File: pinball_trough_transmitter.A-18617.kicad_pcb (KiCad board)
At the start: 2 copper layers, 162.6 x 38.1 mm, 8 parts, among them J1 Conn_01x09_Male

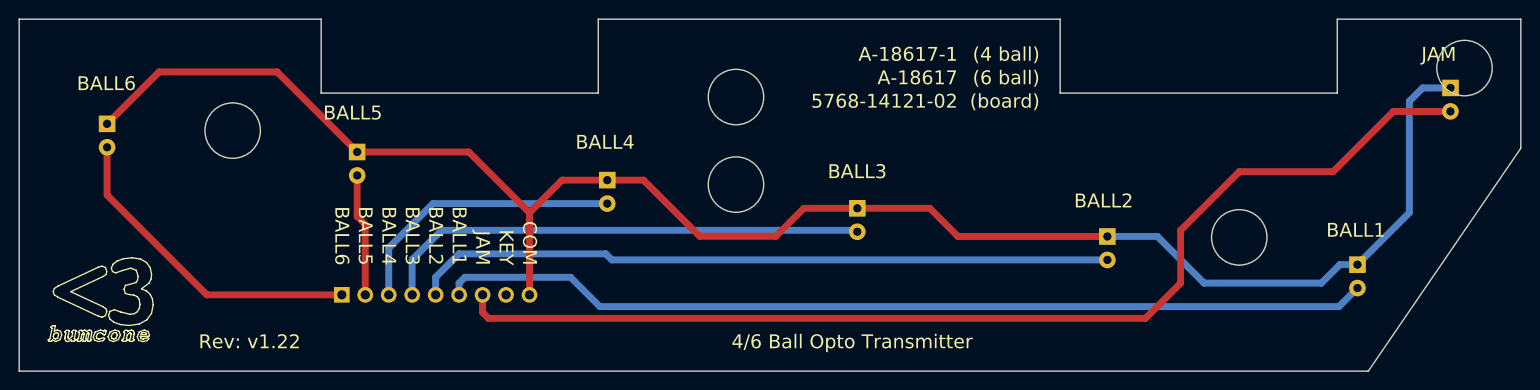
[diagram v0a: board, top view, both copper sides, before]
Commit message: Move JAM LED
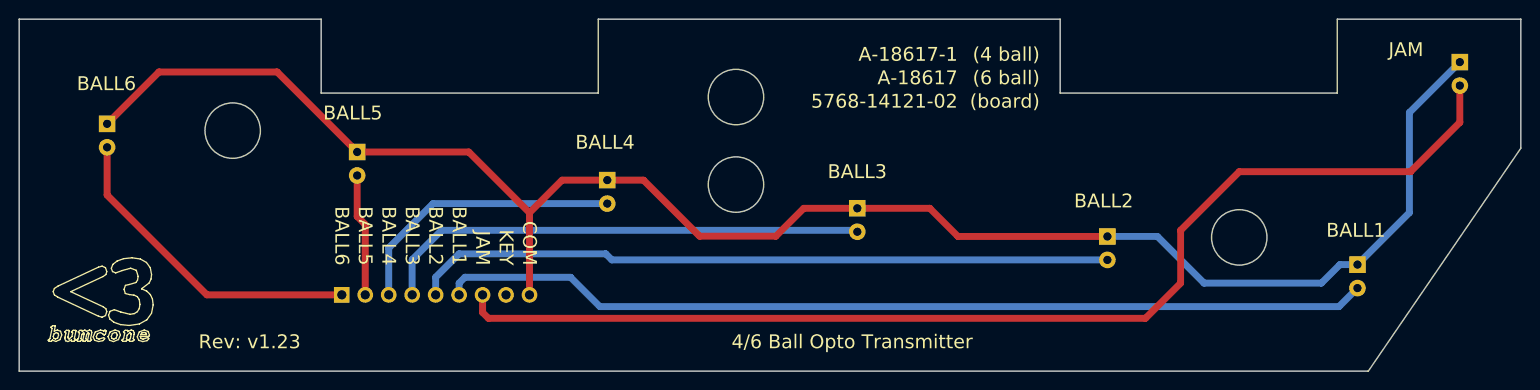
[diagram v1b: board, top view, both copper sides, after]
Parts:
- moved D1 2.97 mm to (219.5, 84.7)
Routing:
- net Net-(D1-Pad2): track 119.6 -> 124.1 mm
- net Net-(D1-Pad1): track 187.3 -> 188.8 mm
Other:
- outline, holes or cut-outs redrawn
- board text added: "Rev: v1.23"
- board text removed: "Rev: v1.22"
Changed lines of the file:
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@@
   (general
     (thickness 1.6)
-    (drawings 602)
-    (tracks 58)
+    (drawings 600)
+    (tracks 57)
     (zones 0)
     (modules 8)
@@
   (page A4)
   (title_block
-    (rev v1.22)
+    (rev v1.23)
   )
   (layers
@@
   )
   (module LED_THT:LED_D5.0mm_Clear (layer B.Cu)
-    (at 218.44 87.455 270)
+    (at 219.456 84.661 270)
     (descr "LED, diameter 5.0mm, 2 pins, http://cdn-reichelt.de/documents/datenblatt/A500/LL-504BC2E-009.pdf")
     (tags "LED diameter 5.0mm 2 pins")
@@
     )
   )
-  (gr_circle (center 219.964 85.304) (end 222.964 85.304) (layer Edge.Cuts) (width 0.15))
   (gr_text "4/6 Ball Opto Transmitter" (at 153.67 114.935) (layer F.SilkS)
     (effects (font (size 1.5 1.5) (thickness 0.3)))
@@
     (effects (font (size 1.5 1.5) (thickness 0.3)) (justify right))
   )
-  (gr_text JAM (at 219.075 83.82) (layer F.SilkS)
+  (gr_text JAM (at 215.519 83.312) (layer F.SilkS)
     (effects (font (size 1.5 1.5) (thickness 0.3)) (justify right))
   )
@@
   (gr_line (start 69.492244 107.223267) (end 68.579256 106.969267) (layer B.SilkS) (width 0.1))
   (gr_line (start 76.835 109.855) (end 76.454 110.107589) (layer B.SilkS) (width 0.1))
-  (gr_text "Rev: v1.22" (at 81.915 114.935) (layer B.SilkS)
+  (gr_text "Rev: v1.23" (at 81.915 114.935) (layer B.SilkS)
     (effects (font (size 1.5 1.5) (thickness 0.3)) (justify right mirror))
   )
@@
     (effects (font (size 1.5 1.5) (thickness 0.3)) (justify right))
   )
-  (gr_text "Rev: v1.22" (at 93.98 114.935) (layer F.SilkS)
-    (effects (font (size 1.5 1.5) (thickness 0.3)) (justify right))
-  )
-  (gr_text JAM (at 214.63 83.82) (layer B.SilkS)
+  (gr_text "Rev: v1.23" (at 93.98 114.935) (layer F.SilkS)
+    (effects (font (size 1.5 1.5) (thickness 0.3)) (justify right))
+  )
+  (gr_text JAM (at 211.074 83.312) (layer B.SilkS)
     (effects (font (size 1.5 1.5) (thickness 0.3)) (justify right mirror))
   )
@@
   (gr_line (start 95.885 107.315) (end 95.885 114.935) (layer B.SilkS) (width 0.2))
   (gr_line (start 120.015 107.315) (end 95.885 107.315) (layer B.SilkS) (width 0.2))
-  (gr_line (start 214.63 84.915) (end 214.63 92.535) (layer B.SilkS) (width 0.15))
-  (gr_line (start 222.25 84.915) (end 214.63 84.915) (layer B.SilkS) (width 0.15))
+  (gr_line (start 215.646 82.121) (end 215.646 89.741) (layer B.SilkS) (width 0.15))
+  (gr_line (start 223.266 82.121) (end 215.646 82.121) (layer B.SilkS) (width 0.15))
   (gr_line (start 204.565 104.14) (end 204.565 111.76) (layer B.SilkS) (width 0.15))
   (gr_line (start 212.185 104.14) (end 204.565 104.14) (layer B.SilkS) (width 0.15))
@@
   (segment (start 165.127 103.532) (end 181.304 103.532) (width 0.75) (layer F.Cu) (net 1))
   (segment (start 162.079 100.484) (end 165.127 103.532) (width 0.75) (layer F.Cu) (net 1))
-  (segment (start 218.44 87.455) (end 215.44 87.455) (width 0.75) (layer B.Cu) (net 1))
-  (segment (start 215.44 87.455) (end 213.995 88.9) (width 0.75) (layer B.Cu) (net 1))
   (segment (start 213.995 100.96) (end 208.375 106.58) (width 0.75) (layer B.Cu) (net 1))
-  (segment (start 213.995 88.9) (end 213.995 100.96) (width 0.75) (layer B.Cu) (net 1))
   (segment (start 206.475 106.58) (end 208.375 106.58) (width 0.75) (layer B.Cu) (net 1))
   (segment (start 204.47 108.585) (end 206.475 106.58) (width 0.75) (layer B.Cu) (net 1))
@@
   (segment (start 186.717 103.532) (end 191.77 108.585) (width 0.75) (layer B.Cu) (net 1))
   (segment (start 181.304 103.532) (end 186.717 103.532) (width 0.75) (layer B.Cu) (net 1))
-  (segment (start 218.44 89.995) (end 212.265 89.995) (width 0.75) (layer F.Cu) (net 2))
-  (segment (start 212.265 89.995) (end 205.74 96.52) (width 0.75) (layer F.Cu) (net 2))
-  (segment (start 205.74 96.52) (end 195.58 96.52) (width 0.75) (layer F.Cu) (net 2))
+  (segment (start 213.995 90.122) (end 219.456 84.661) (width 0.75) (layer B.Cu) (net 1))
+  (segment (start 213.995 100.96) (end 213.995 90.122) (width 0.75) (layer B.Cu) (net 1))
   (segment (start 195.58 96.52) (end 189.23 102.87) (width 0.75) (layer F.Cu) (net 2))
   (segment (start 189.23 102.87) (end 189.23 108.585) (width 0.75) (layer F.Cu) (net 2))
@@
   (segment (start 113.665 111.76) (end 113.665 109.855) (width 0.75) (layer F.Cu) (net 2))
   (segment (start 114.3 112.395) (end 113.665 111.76) (width 0.75) (layer F.Cu) (net 2))
+  (segment (start 195.58 96.52) (end 214.122 96.52) (width 0.75) (layer F.Cu) (net 2))
+  (segment (start 219.456 91.186) (end 219.456 87.201) (width 0.75) (layer F.Cu) (net 2))
+  (segment (start 214.122 96.52) (end 219.456 91.186) (width 0.75) (layer F.Cu) (net 2))
   (segment (start 206.37 111.125) (end 208.375 109.12) (width 0.75) (layer B.Cu) (net 3))
   (segment (start 126.365 111.125) (end 123.19 107.95) (width 0.75) (layer B.Cu) (net 3))

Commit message: Move J1 header back a little
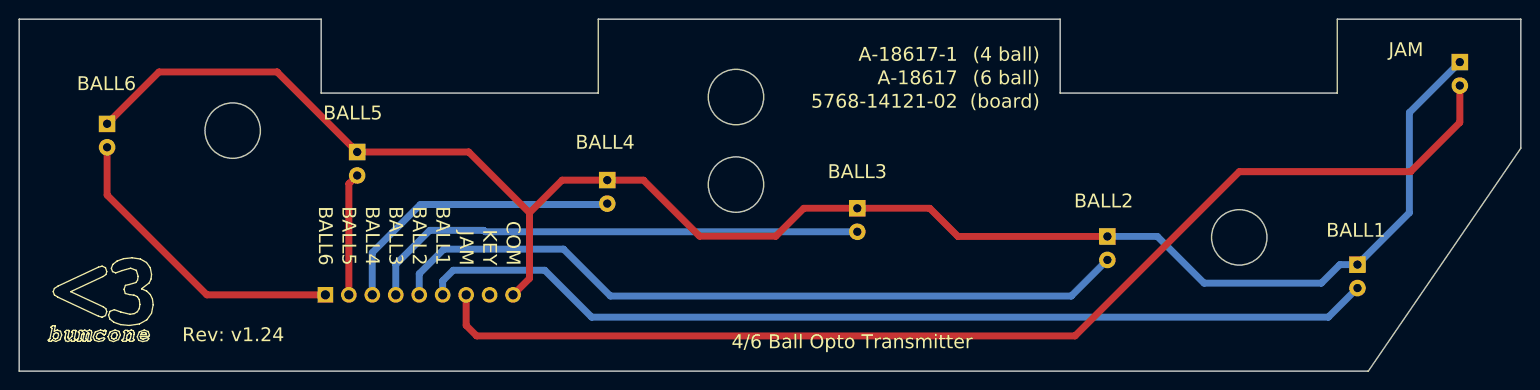
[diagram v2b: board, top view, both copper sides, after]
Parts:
- moved J1 1.78 mm to (96.6, 109.9)
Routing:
- net Net-(D3-Pad2): track 76.0 -> 81.6 mm
- net Net-(D2-Pad2): track 100.9 -> 104.4 mm
- net Net-(D7-Pad2): track 35.1 -> 33.3 mm
- net Net-(D4-Pad2): track 53.4 -> 55.1 mm
- net Net-(D5-Pad2): track 30.7 -> 32.2 mm
- net Net-(D1-Pad2): track 124.1 -> 124.9 mm
- net Net-(D1-Pad1): track 188.8 -> 189.5 mm
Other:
- board text added: "Rev: v1.24"
- board text removed: "Rev: v1.23"

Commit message: Use Molex connector
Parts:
- J1: value Conn_01x09_Male -> Molex 22-05-3091
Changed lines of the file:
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@@
       (effects (font (size 1 1) (thickness 0.15)) (justify mirror))
     )
-    (fp_text value Conn_01x09_Male (at -3.175 -9.525) (layer B.Fab)
+    (fp_text value "Molex 22-05-3091" (at -3.175 -9.525) (layer B.Fab)
       (effects (font (size 1 1) (thickness 0.15)) (justify mirror))
     )
@@
     (pad 1 thru_hole rect (at 0 0 270) (size 1.7 1.7) (drill 1) (layers *.Cu *.Mask)
       (net 8 "Net-(D7-Pad2)"))
-    (model ${KISYS3DMOD}/Connector_PinHeader_2.54mm.3dshapes/PinHeader_1x09_P2.54mm_Horizontal.wrl
+    (model ${KIPRJMOD}/kicad/libs/packages3d/Molex/22-05-3091.step
       (at (xyz 0 0 0))
       (scale (xyz 1 1 1))

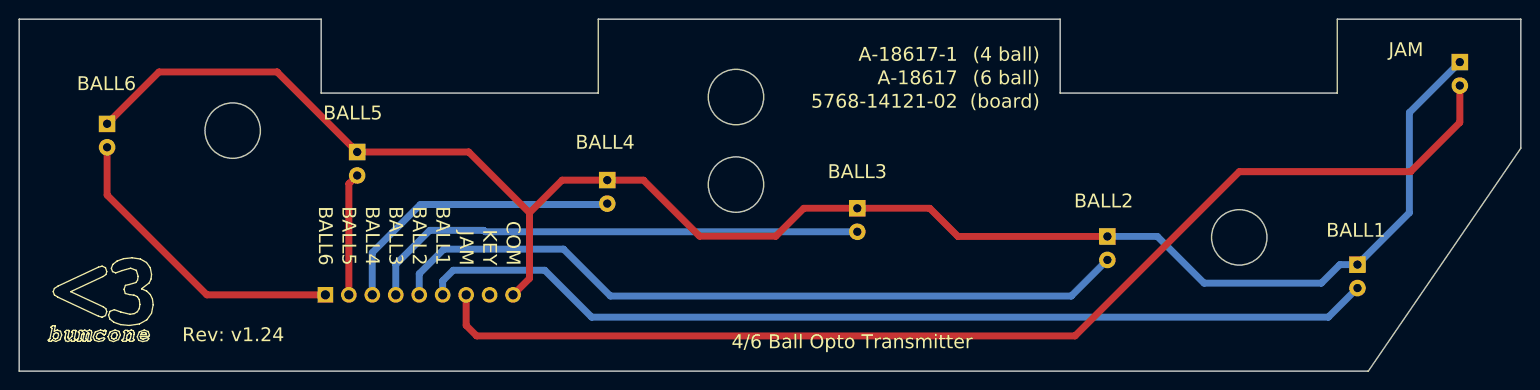
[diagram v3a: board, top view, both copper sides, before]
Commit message: Align LEDs with the center of the trough holes
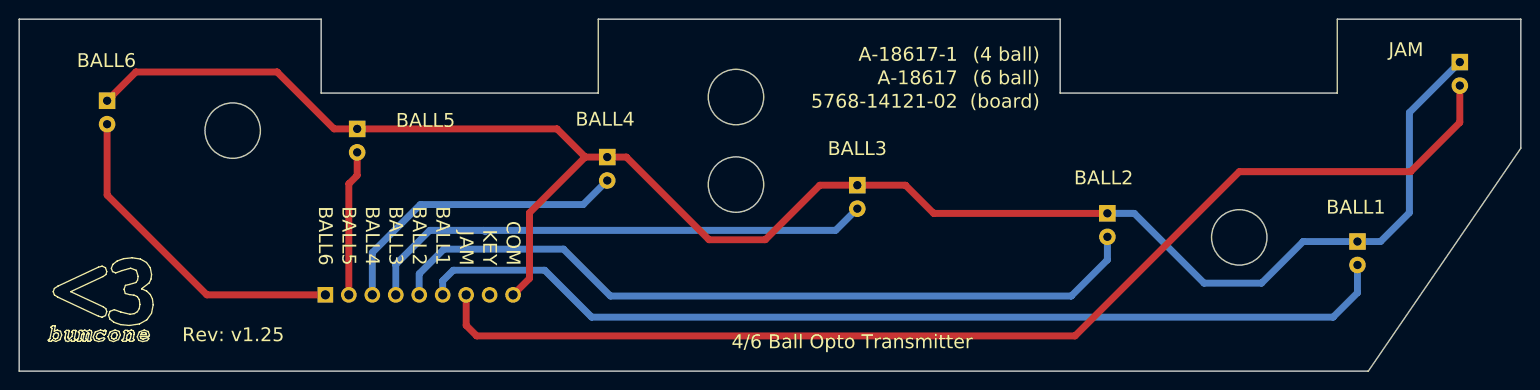
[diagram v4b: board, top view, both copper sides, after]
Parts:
- moved D2 2.50 mm to (208.4, 104.1)
- moved D3 2.50 mm to (181.3, 101.0)
- moved D4 2.50 mm to (154.2, 98.0)
- moved D5 2.50 mm to (127.2, 94.9)
- moved D6 2.50 mm to (100.1, 91.9)
- moved D7 2.50 mm to (73.0, 88.8)
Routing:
- net Net-(D1-Pad1): track 189.5 -> 196.5 mm
- net Net-(D2-Pad2): track 104.4 -> 107.2 mm
- net Net-(D7-Pad2): track 33.3 -> 35.8 mm
- net Net-(D6-Pad2): track 13.3 -> 15.8 mm
- net Net-(D3-Pad2): track 81.6 -> 84.1 mm
- net Net-(D5-Pad2): track 32.2 -> 33.4 mm
- net Net-(D4-Pad2): track 55.1 -> 56.2 mm
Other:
- board text added: "Rev: v1.25"
- board text removed: "Rev: v1.24"

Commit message: Minor board rearranging
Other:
- rule pad_to_mask_clearance: 0.051 -> 0
- board text added: "Rev: v1.26"
- board text removed: "Rev: v1.25"
